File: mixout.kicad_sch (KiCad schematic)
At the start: 42 parts, among them J1 AudioJack2, J2 Conn_02x05_Odd_Even, J3 Conn_02x04_Odd_Even, Q1 BCM847, Q2 BCM847, U1 TL074, U2 TL072

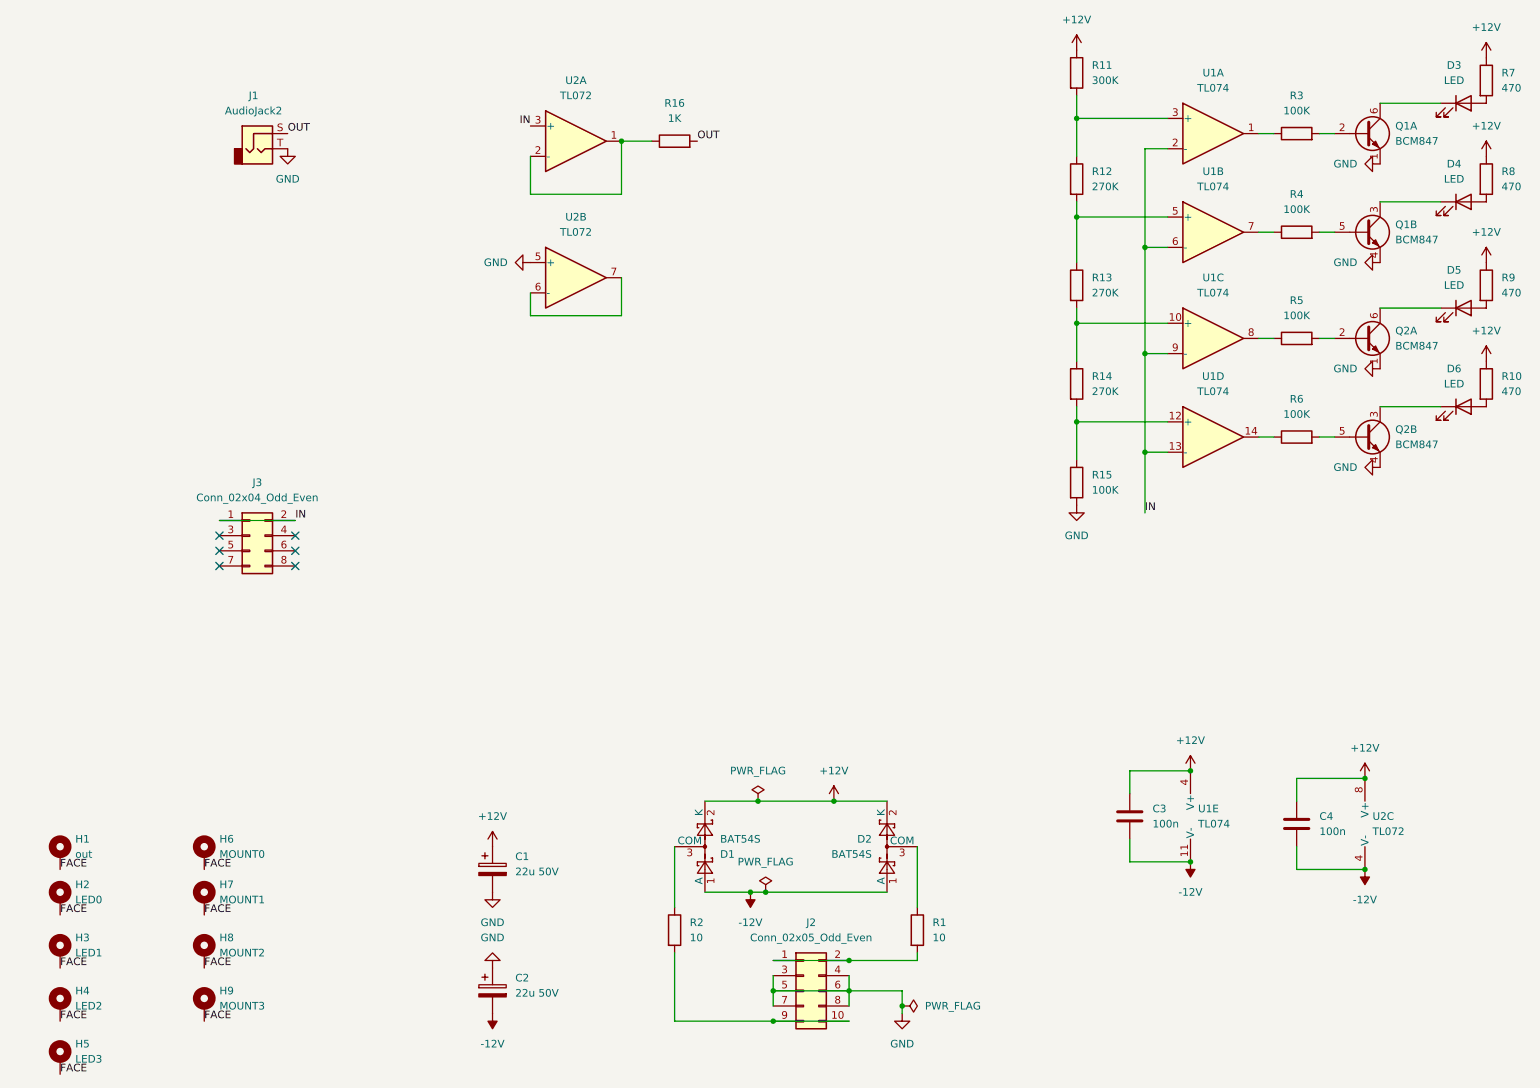
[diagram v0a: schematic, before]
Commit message: pcb layed out
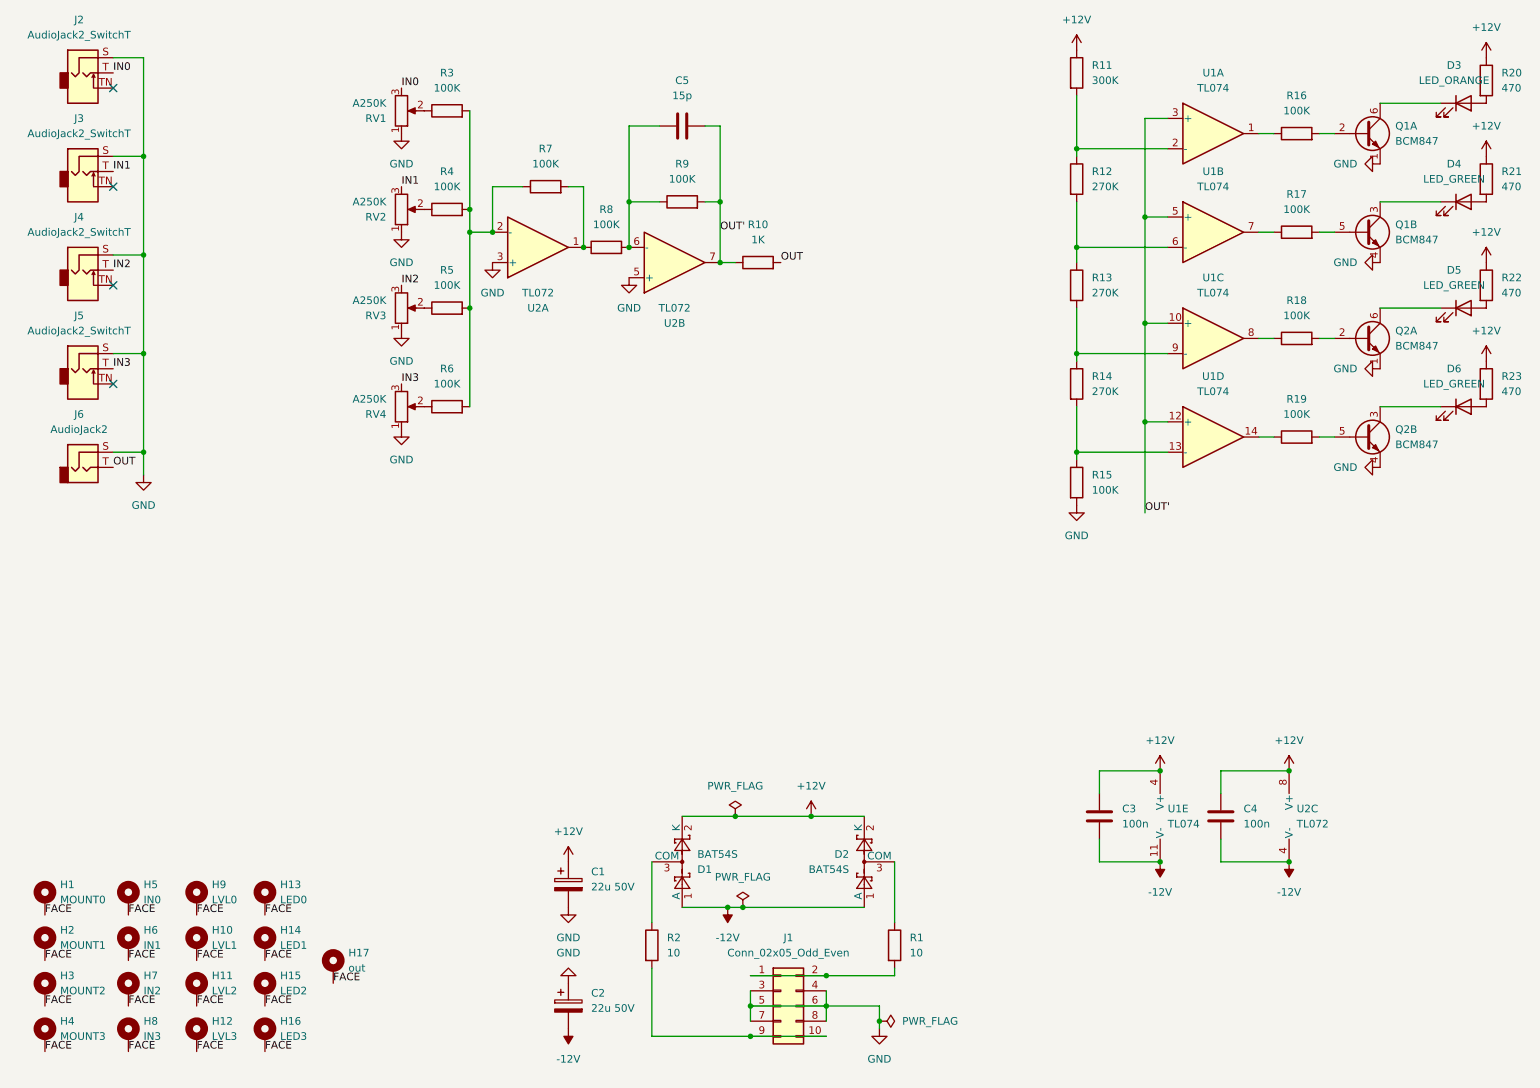
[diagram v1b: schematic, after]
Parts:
- removed J3: Conn_02x04_Odd_Even, symbol Connector_Generic:Conn_02x04_Odd_Even
- removed R16: 1K, symbol Device:R
- added C5: 15p, Capacitor_SMD:C_0805_2012Metric, symbol Device:C
- added H10: LVL1, Eurorack:Mech-Potentiometer-Hole_level_90deg, symbol Mechanical:MountingHole_Pad
- added H11: LVL2, Eurorack:Mech-Potentiometer-Hole_level_90deg, symbol Mechanical:MountingHole_Pad
- added H12: LVL3, Eurorack:Mech-Potentiometer-Hole_level_90deg, symbol Mechanical:MountingHole_Pad
- added H5: IN0, Eurorack:Mech-AudioJack-Hole, symbol Mechanical:MountingHole_Pad
- added H6: IN1, Eurorack:Mech-AudioJack-Hole, symbol Mechanical:MountingHole_Pad
- added H7: IN2, Eurorack:Mech-AudioJack-Hole, symbol Mechanical:MountingHole_Pad
- added H8: IN3, Eurorack:Mech-AudioJack-Hole, symbol Mechanical:MountingHole_Pad
- added H9: LVL0, Eurorack:Mech-Potentiometer-Hole_level_90deg, symbol Mechanical:MountingHole_Pad
- added J2, J3, J4, J5: AudioJack2_SwitchT, Eurorack:AudioJack2_Tayda_A-2566, symbol Eurorack:AudioJack2_SwitchT
- added R10: 1K, Resistor_SMD:R_0805_2012Metric, symbol Device:R
- added R3, R4, R5, R6, R7, R8, R9: 100K, Resistor_SMD:R_0805_2012Metric, symbol Device:R
- added RV1, RV2, RV3, RV4: A250K, Eurorack:Potentiometer_RV16AF-41-15R1, symbol Device:R_Potentiometer
- C1, C2: footprint (none) -> Capacitor_THT:CP_Radial_D5.0mm_P2.50mm
- C3, C4: footprint (none) -> Capacitor_SMD:C_0805_2012Metric
- D3: value LED -> LED_ORANGE; footprint (none) -> LED_THT:LED_D3.0mm
- D4, D5, D6: value LED -> LED_GREEN; footprint (none) -> LED_THT:LED_D3.0mm
- H1: renamed from H6; footprint (none) -> Eurorack:Mech-MountingHole
- H13: renamed from H2; footprint (none) -> Eurorack:Mech-LED-Hole-3mm-Bezel
- H14: renamed from H3; footprint (none) -> Eurorack:Mech-LED-Hole-3mm-Bezel
- H15: renamed from H4; footprint (none) -> Eurorack:Mech-LED-Hole-3mm-Bezel
- H16: renamed from H5; footprint (none) -> Eurorack:Mech-LED-Hole-3mm-Bezel
- H17: renamed from H1; footprint (none) -> Eurorack:Mech-Hole-10mm
- H2: renamed from H7; footprint (none) -> Eurorack:Mech-MountingHole
- H3: renamed from H8; footprint (none) -> Eurorack:Mech-MountingHole
- H4: renamed from H9; footprint (none) -> Eurorack:Mech-MountingHole
- J1: renamed from J2; footprint (none) -> Eurorack:PinHeader_2x05_P2.54mm_Vertical
- J6: renamed from J1; footprint (none) -> Eurorack:AudioJack2_Tayda_A-1009
- Q1, Q2: footprint (none) -> Package_SO:TSOP-6_1.65x3.05mm_P0.95mm
- R1, R11, R12, R13, R14, R15, R2: footprint (none) -> Resistor_SMD:R_0805_2012Metric
- R16: renamed from R3; footprint (none) -> Resistor_SMD:R_0805_2012Metric
- R17: renamed from R4; footprint (none) -> Resistor_SMD:R_0805_2012Metric
- R18: renamed from R5; footprint (none) -> Resistor_SMD:R_0805_2012Metric
- R19: renamed from R6; footprint (none) -> Resistor_SMD:R_0805_2012Metric
- R20: renamed from R7; footprint (none) -> Resistor_SMD:R_0805_2012Metric
- R21: renamed from R8; footprint (none) -> Resistor_SMD:R_0805_2012Metric
- R22: renamed from R9; footprint (none) -> Resistor_SMD:R_0805_2012Metric
- R23: renamed from R10; footprint (none) -> Resistor_SMD:R_0805_2012Metric
- U1: footprint (none) -> Package_SO:SOIC-14_3.9x8.7mm_P1.27mm
- U2: footprint (none) -> Package_SO:SOIC-8_3.9x4.9mm_P1.27mm
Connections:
- net FACE: now also H10.1, H11.1, H12.1, H5.1, H6.1, H7.1, H8.1, H9.1
- net GND: now also J6.S, U2.3 (+), J2.S, J3.S, J4.S, J5.S, RV1.1, RV2.1, RV3.1, RV4.1; no longer J6.T
- net OUT: now also J6.T, R10.2; no longer J6.S
- net at R11.2, R12.1: now also U1.2 (-); no longer U1.3 (+)
- net at R13.2, R14.1: now also U1.9 (-); no longer U1.10 (+)
- net at R12.2, R13.1: now also U1.6 (-); no longer U1.5 (+)
- net at R14.2, R15.1: now also U1.13 (-); no longer U1.12 (+)
- net at U2.2 (-): now also R3.2, R4.2, R5.2, R6.2, R7.1; no longer U2.1
- net at U2.6 (-): now also C5.2, R8.2, R9.1; no longer U2.7
- removed net IN: U1.13 (-), U1.2 (-), U1.6 (-), U1.9 (-), U2.3 (+)
- new net: R5.1, RV3.2
- new net: R6.1, RV4.2
- new net: R7.2, R8.1, U2.1
- new net: R3.1, RV1.2
- new net: R4.1, RV2.2
- new net IN0: J2.T, RV1.3
- new net IN1: J3.T, RV2.3
- new net IN2: J4.T, RV3.3
- new net IN3: J5.T, RV4.3
- new net OUT': C5.1, R10.1, R9.2, U1.10 (+), U1.12 (+), U1.3 (+), U1.5 (+), U2.7
- no-connect marks 6 -> 4
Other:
- moved on the sheet: C1, C2, C3, C4, D1, D2, H1, H13, H14, H15, H16, H17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
